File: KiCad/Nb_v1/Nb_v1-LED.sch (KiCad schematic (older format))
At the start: 161 parts, among them K2 LED_ENABLE, Q1 2N5401, Q10 2N5401, Q11 2N5401, Q12 2N5401, Q13 2N5401, Q14 2N5401, Q15 2N5401, Q16 2N5401, Q2 2N5401, Q3 2N5401, Q4 2N5401, Q5 2N5401, Q6 2N5401, Q7 2N5401, Q8 2N5401, Q9 2N5401

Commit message: Nb_v1 Nachbau Schematic
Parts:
- removed K2: LED_ENABLE, pin_strip_3, symbol CONN_3
- removed Q1, Q10, Q11, Q12, Q13, Q14, Q15, Q16, Q2, Q3, Q4, Q5, Q6, Q7, Q8, Q9: 2N5401, to92_2N5401, symbol PNP
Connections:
- net labels added: R09, R10
- net labels removed: COL12, COL13, COL14, COL15, COL16, VCC
- wire segments 382 -> 402
- no-connect marks 1 -> 0
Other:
- moved on the sheet: D100, D101, D102, D103, D104, D105, D106, D107, D108, D109, D110, D111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

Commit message: NachBau Schematic update
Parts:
- removed D126, D127, D128: LED, led_5mm_clear, symbol LED
- removed R1, R10, R11, R12, R13, R14, R15, R16, R2, R3, R4, R5, R6, R7, R8, R9: 100, RC03, symbol R
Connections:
- net labels added: +1M, +2M, +3M, +4M, R11, VCC
- wire segments 402 -> 300
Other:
- moved on the sheet: D111, D112, D113, D114, D115, D116, D117, D118, D119, D120, D121

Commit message: Nachbau Schematic updates. Seems close to final.
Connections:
- wire segments 300 -> 294
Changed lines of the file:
@@
-EESchema Schematic File Version 2  date Thu 24 Nov 2011 11:40:31 PM IST
+EESchema Schematic File Version 2  date 11/25/2011 1:26:45 PM
 LIBS:Nb_v1
 LIBS:power
@@
 encoding utf-8
 Sheet 2 4
-Title "ClockTHREE Junior aka C3Jr"
-Date "24 nov 2011"
+Title "NachBau - WordClock"
+Date "25 nov 2011"
 Rev "A"
-Comp "an improved WordClock based on ClockTHREE"
+Comp ""
 Comment1 "www.wyolum.com"
 Comment2 "wyojustin@gmail.com :: anool.m@gmail.com"
-Comment3 "part of the project inspired from : http://www.evilmadscientist.com/article.php/peggy2"
+Comment3 ""
 Comment4 ""
 $EndDescr
@@
 	2850 1050 2550 1050
 Wire Wire Line
-	9950 9850 9950 9900
-Wire Wire Line
-	9150 9850 9150 9900
-Wire Wire Line
-	8350 9850 8350 9900
-Wire Wire Line
-	7550 9850 7550 9900
-Wire Wire Line
-	6750 9850 6750 9900
-Wire Wire Line
-	5950 9850 5950 9900
-Wire Wire Line
 	3350 1050 3650 1050

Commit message: Nachbau, started initial spade work on PCB
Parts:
- added P17: CONN_4X2, pin_array_4x2, symbol CONN_4X2
- added P18, P19: CONN_12, pin_array_12x1, symbol CONN_12
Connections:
- net +1M renamed 1M
- net 1M: now also P17.1
- net +2M renamed 2M
- net 2M: now also P17.3
- net +3M renamed 3M
- net 3M: now also P17.5
- net +4M renamed 4M
- net 4M: now also P17.7
- net COL01 renamed K01
- net K01: now also P18.1
- net COL02 renamed K02
- net K02: now also P18.2
- net COL03 renamed K03
- net K03: now also P18.3
- net COL04 renamed K04
- net K04: now also P18.4
- net COL05 renamed K05
- net K05: now also P18.5
- net COL06 renamed K06
- net K06: now also P18.6
- net COL07 renamed K07
- net K07: now also P18.7
- net COL08 renamed K08
- net K08: now also P18.8
- net COL09 renamed K09
- net K09: now also P18.9
- net COL10 renamed K10
- net K10: now also P18.10
- net COL11 renamed K11
- net K11: now also P18.11
- net R01 renamed A01
- net A01: now also P19.1
- net R02 renamed A02
- net A02: now also P19.2
- net R03 renamed A03
- net A03: now also P19.3
- net R04 renamed A04
- net A04: now also P19.4
- net R05 renamed A05
- net A05: now also P19.5
- net R06 renamed A06
- net A06: now also P19.6
- net R07 renamed A07
- net A07: now also P19.7
- net R08 renamed A08
- net A08: now also P19.8
- net R09 renamed A09
- net A09: now also P19.9
- net R10 renamed A10
- net A10: now also P19.10
- net R11 renamed A11
- net A11: now also P19.11
- net VCC renamed +CM
- net +CM: now also P17.2, P17.4, P17.6, P17.8
- no-connect marks 0 -> 2

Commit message: Nachbau update, some more work on board
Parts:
- D1, D2: footprint led_5mm_clear -> d_0805
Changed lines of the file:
@@
-EESchema Schematic File Version 2  date 11/25/2011 7:19:25 PM
+EESchema Schematic File Version 2  date Fri 25 Nov 2011 10:46:27 PM IST
 LIBS:Nb_v1
 LIBS:power
@@
 F 0 "D1" H 2950 1800 50  0000 C CNN
 F 1 "LED" H 2950 1600 50  0000 C CNN
-F 2 "led_5mm_clear" H 2950 1700 60  0001 C CNN
+F 2 "d_0805" H 2950 1700 60  0001 C CNN
 	1    2950 1700
 	0    -1   -1   0
@@
 F 0 "D2" H 3750 1800 50  0000 C CNN
 F 1 "LED" H 3750 1600 50  0000 C CNN
-F 2 "led_5mm_clear" H 3750 1700 60  0001 C CNN
+F 2 "d_0805" H 3750 1700 60  0001 C CNN
 	1    3750 1700
 	0    -1   -1   0

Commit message: Nachbau Schematic almost final, working on PCB component layout first
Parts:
- D1, D2: footprint d_0805 -> led_5mm_clear
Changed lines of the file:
@@
-EESchema Schematic File Version 2  date Fri 25 Nov 2011 10:46:27 PM IST
+EESchema Schematic File Version 2  date 11/26/2011 1:49:00 PM
 LIBS:Nb_v1
 LIBS:power
-LIBS:conn
 LIBS:Nb_v1-cache
 EELAYER 25  0
@@
 Sheet 2 4
 Title "NachBau - WordClock"
-Date "25 nov 2011"
+Date "26 nov 2011"
 Rev "A"
 Comp ""
@@
 F 0 "D1" H 2950 1800 50  0000 C CNN
 F 1 "LED" H 2950 1600 50  0000 C CNN
-F 2 "d_0805" H 2950 1700 60  0001 C CNN
+F 2 "led_5mm_clear" H 2950 1700 60  0001 C CNN
 	1    2950 1700
 	0    -1   -1   0
@@
 F 0 "D2" H 3750 1800 50  0000 C CNN
 F 1 "LED" H 3750 1600 50  0000 C CNN
-F 2 "d_0805" H 3750 1700 60  0001 C CNN
+F 2 "led_5mm_clear" H 3750 1700 60  0001 C CNN
 	1    3750 1700
 	0    -1   -1   0

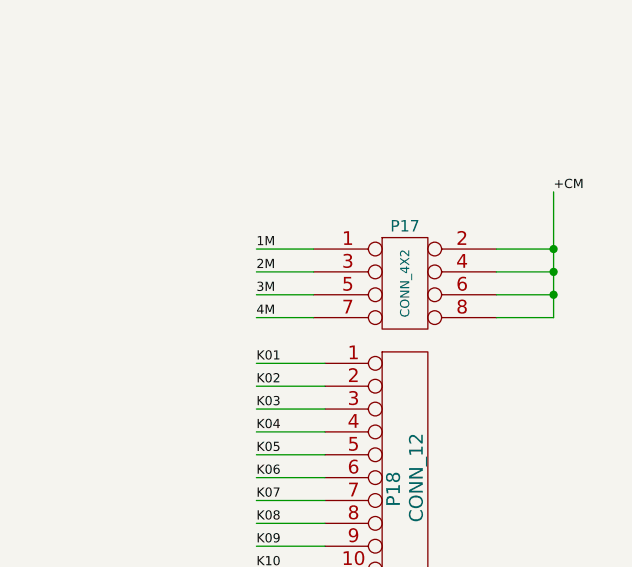
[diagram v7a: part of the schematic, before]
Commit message: Nachbau Board layout (LED Matrix removed - make a separate Board for LEDs)
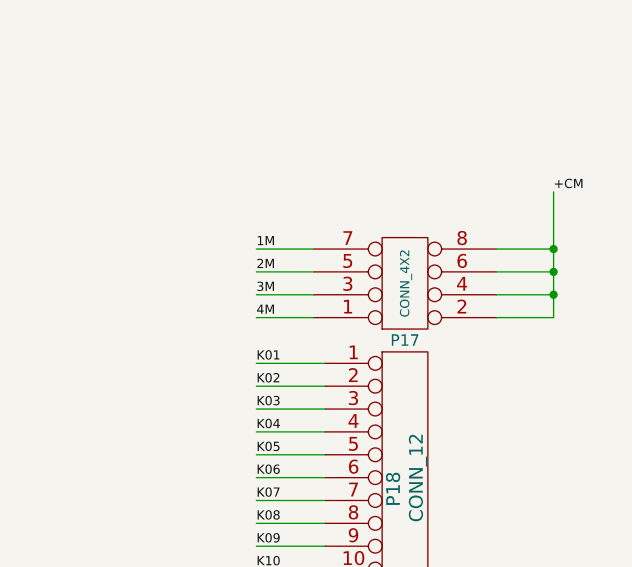
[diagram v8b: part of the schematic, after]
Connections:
- net 1M: now also P17.7; no longer P17.1
- net 2M: now also P17.5; no longer P17.3
- net 3M: now also P17.3; no longer P17.5
- net 4M: now also P17.1; no longer P17.7
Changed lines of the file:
@@
-EESchema Schematic File Version 2  date 11/26/2011 1:49:00 PM
+EESchema Schematic File Version 2  date Sun 27 Nov 2011 12:00:12 AM IST
 LIBS:Nb_v1
 LIBS:power
@@
 $Descr A3 16535 11700
 encoding utf-8
-Sheet 2 4
+Sheet 2 3
 Title "NachBau - WordClock"
 Date "26 nov 2011"
@@
 F 2 "pin_array_4x2" H 13000 4350 60  0001 C CNN
 	1    13000 4350
-	1    0    0    -1
+	1    0    0    1
 $EndComp
 $Comp
